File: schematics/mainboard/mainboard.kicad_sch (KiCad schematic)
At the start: 90 parts, among them J1 SD_Card_Receptacle, J2 LCD_CONN, J3 USB_C_Receptacle_USB2.0_16P, J4 BATTERY_CONN, J5 Conn_01x03_Pin, J6 HID_CONN, J7 AudioJack3_Switch, J8 TRACKBALL_CONN, P1 1-1473005-4, SW1 SW_SPST, U1 AMS1117-3.3, U2 AMS1117-3.3, U3 MAX3421EETJ_T, U6 TPS63002, U7 BQ24072RGT, U8 MAX9715xTE+, Y1 12MHz

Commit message: Updated mainboard to use I2S audio.
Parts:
- removed C21, C22, C23, C24: 10nF, Capacitor_SMD:C_0805_2012Metric_Pad1.18x1.45mm_HandSolder, symbol pspice:C
- removed C26: 47uF, Capacitor_Tantalum_SMD:CP_EIA-3216-18_Kemet-A, symbol Device:C_Polarized
- removed J5: Conn_01x03_Pin, Connector_PinHeader_2.54mm:PinHeader_1x03_P2.54mm_Vertical, symbol Connector:Conn_01x03_Pin
- removed J7: AudioJack3_Switch, symbol Connector_Audio:AudioJack3_Switch
- removed LS1, LS2: Speaker, symbol Device:Speaker
- removed R20: 4k7, Resistor_SMD:R_0805_2012Metric_Pad1.20x1.40mm_HandSolder, symbol Device:R
- removed U8: MAX9715xTE+, Package_DFN_QFN:TQFN-16-1EP_5x5mm_P0.8mm_EP3.1x3.1mm, symbol Amplifier_Audio:MAX9715xTE+
- added C21, C23, C26, C35, C36: 0.1uF, Capacitor_SMD:C_0805_2012Metric_Pad1.18x1.45mm_HandSolder, symbol Device:C
- added C22, C24, C33, C37: 10uF, Capacitor_SMD:C_0805_2012Metric_Pad1.18x1.45mm_HandSolder, symbol Device:C
- added C34, C38: 22uF, Capacitor_SMD:C_0805_2012Metric_Pad1.18x1.45mm_HandSolder, symbol Device:C
- added J7: Conn_01x02_Pin, Connector_PinHeader_2.54mm:PinHeader_1x02_P2.54mm_Vertical, symbol Connector:Conn_01x02_Pin
- added J9: AudioJack3, Connector_Audio:Jack_3.5mm_Switronic_ST-005-G_horizontal, symbol Connector_Audio:AudioJack3
- added U5: AMS1117-1.8, Package_TO_SOT_SMD:SOT-223-3_TabPin2, symbol Regulator_Linear:AMS1117-1.8
- added U8: ~, MY_AUDIO:QFN50P500X500X100-33N, symbol 6PA3100IRHBRQ1:6PA3100IRHBRQ1
- C15, C32: value 1uF -> 0.1uF; footprint Capacitor_SMD:C_0805_2012Metric -> Capacitor_SMD:C_0805_2012Metric_Pad1.18x1.45mm_HandSolder; LCSC (none) -> C28233
- C5: value 1uF -> 10uF; footprint Capacitor_SMD:C_0805_2012Metric -> Capacitor_SMD:C_0805_2012Metric_Pad1.18x1.45mm_HandSolder; LCSC (none) -> C1713
- R17, R18, R19: LCSC (none) -> C17673
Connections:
- net 3V3_LCD is gone; now on net 3V3_AUDIO: C2.1, C3.2, C4.2, J1.4 (VDD), J2.1 (Pin_1), J2.17 (Pin_17), R21.2, R22.2, R23.2, R24.2, R25.2, R29.2, U1.2 (VO)
- net PWM_L is gone; now on net 3V3_AUDIO: R17.1
- net PWM_R is gone; now on net 3V3_AUDIO: R18.1
- net 5V0: now also C32.1, C34.1, C36.1, C38.1, U8.21 (SPKVDD), U8.24 (SPKVDD); no longer C32.2, C5.2
- net GND: now also C25.2, C32.2, C5.2, C21.2, C22.2, C23.2, C24.2, C26.2, C33.2, C34.2, C35.2, C36.2, C37.2, C38.2, J9.S, U5.1 (GND), U8.1 (IOVSS), U8.13 (AIN1), U8.14 (AIN2), U8.16 (AVSS), U8.18 (DVSS), U8.20 (SPKVSS), U8.25 (SPKVSS), U8.29 (HPVSS); no longer C32.1, C5.1
- net 3V3_AUDIO: now reaches R19.1
- net 3V3_AUDIO: now also C5.1, C23.1, C24.1, C26.1, C33.1, C35.1, C37.1, U5.3 (VI), U8.17 (AVDD), U8.2 (IOVDD), U8.28 (HPVDD); no longer R17.2
- net 1V8: now reaches C25.1
- net 1V8: now also C21.1, C22.1, U5.2 (VO), U8.3 (DVDD); no longer R19.2
- net ~{RESET}: now reaches C15.1
- net ~{RESET}: now also R17.2, U8.31 (~{RESET})
- net AUDIO_SDA: now reaches R18.2
- net AUDIO_SDA: now also U8.9 (SDA)
- new net: J9.R, U8.30 (HPR)
- new net: J9.T, U8.27 (HPL)
- new net: J7.1 (Pin_1), U8.19 (SPKM), U8.23 (SPKM)
- new net: J7.2 (Pin_2), U8.22 (SPKP), U8.26 (SPKP)
- new net AUDIO_BCLK: U8.7 (BCLK)
- new net AUDIO_DIN: U8.5 (DIN)
- new net AUDIO_MCLK: U8.8 (MCLK)
- new net AUDIO_SCL: R19.2, U8.10 (SCL)
- new net AUDIO_WCLK: U8.6 (WCLK)
- new net GPIO1: U8.32 (GPIO1)
- new net VOL/MICDET: U8.11 (VOL/MICDET)
- no-connect marks 72 -> 74
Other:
- note added: "AUDIO"
- note added: "BATTERY MNGR"
- note added: "INPUT CONNECTORS"
- note added: "LCD CONNECTOR"
- note added: "REGULATORS"
- note added: "SD CARD"
- note added: "SRAM"
- note added: "USB INTERFACE"
- moved on the sheet: C1, C10, C11, C12, C13, C14, C16, C17, C18, C2, C25, C27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

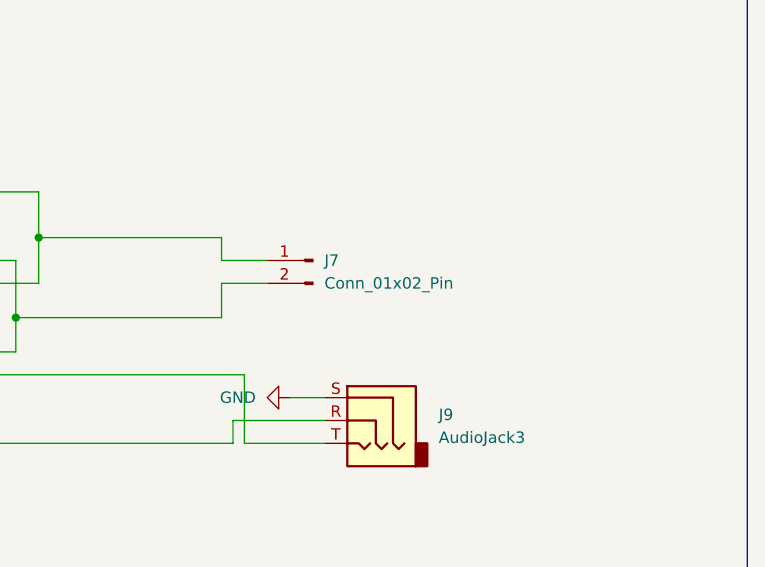
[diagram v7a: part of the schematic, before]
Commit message: Mainboard work, trying to figure out optimal outline.
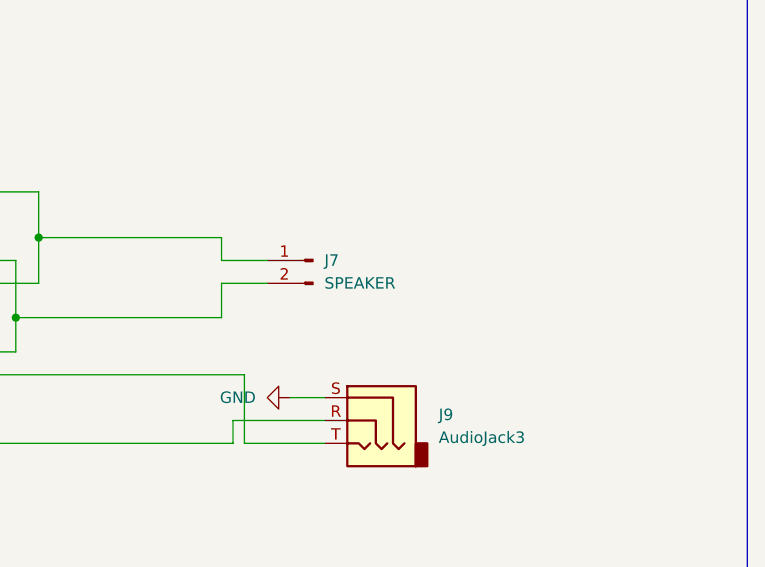
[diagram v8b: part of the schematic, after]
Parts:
- J7: value Conn_01x02_Pin -> SPEAKER
- SW1: footprint Connector_PinHeader_1.00mm:PinHeader_1x02_P1.00mm_Vertical -> Connector_PinHeader_2.54mm:PinHeader_1x02_P2.54mm_Vertical
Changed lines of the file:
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@@
 			)
 		)
-		(property "Footprint" "Connector_PinHeader_1.00mm:PinHeader_1x02_P1.00mm_Vertical"
+		(property "Footprint" "Connector_PinHeader_2.54mm:PinHeader_1x02_P2.54mm_Vertical"
 			(at 165.1 436.88 0)
 			(effects
@@
 			)
 		)
-		(property "Value" "Conn_01x02_Pin"
+		(property "Value" "SPEAKER"
 			(at 769.62 167.6399 0)
 			(effects
